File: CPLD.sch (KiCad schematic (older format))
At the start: 35 parts, among them J5 JTAG, SW2 SW_DIP_x06, SW3 User PB, U12 74HCT3G04, U3 EPM7064STC100, X1 CFPS-72 50mhz

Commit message: lots of fixes
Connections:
- net labels added: IEI, IEO
- wire segments 186 -> 187
- no-connect marks 8 -> 6
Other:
- moved on the sheet: C5, D2, J5, R10, R11, R12, R13, R15, R16, R17, R18, RN1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

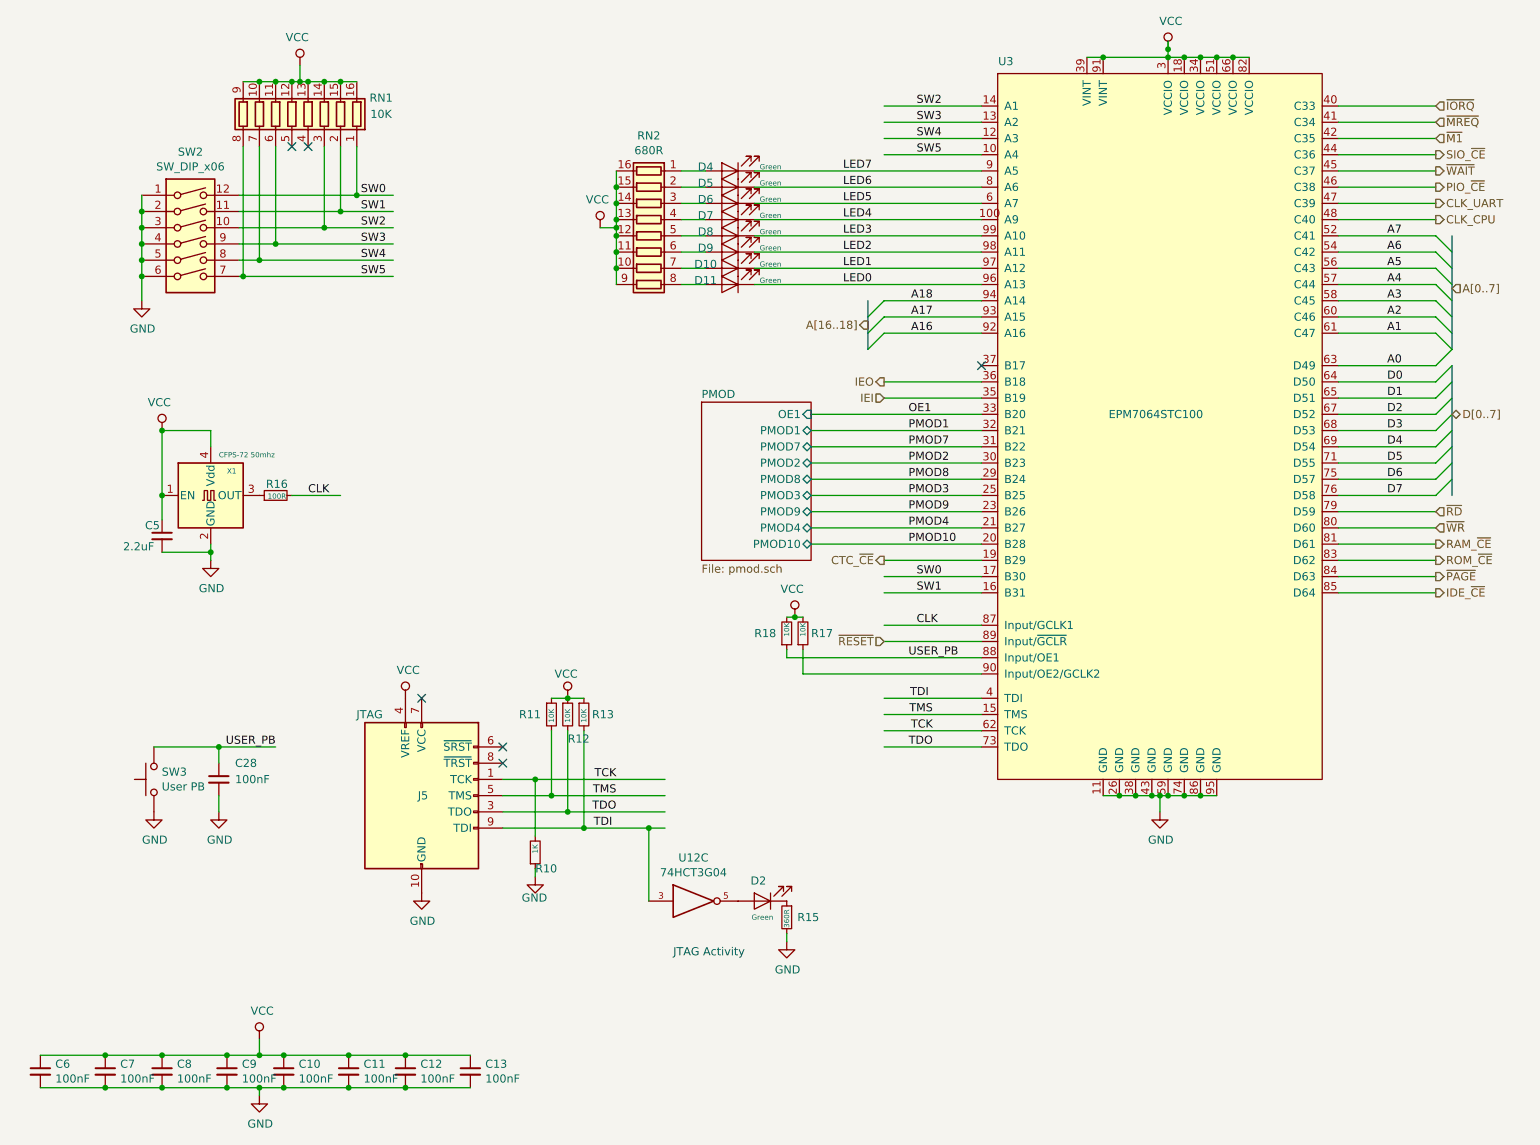
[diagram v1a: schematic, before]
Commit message: fixed led values, added pwr led
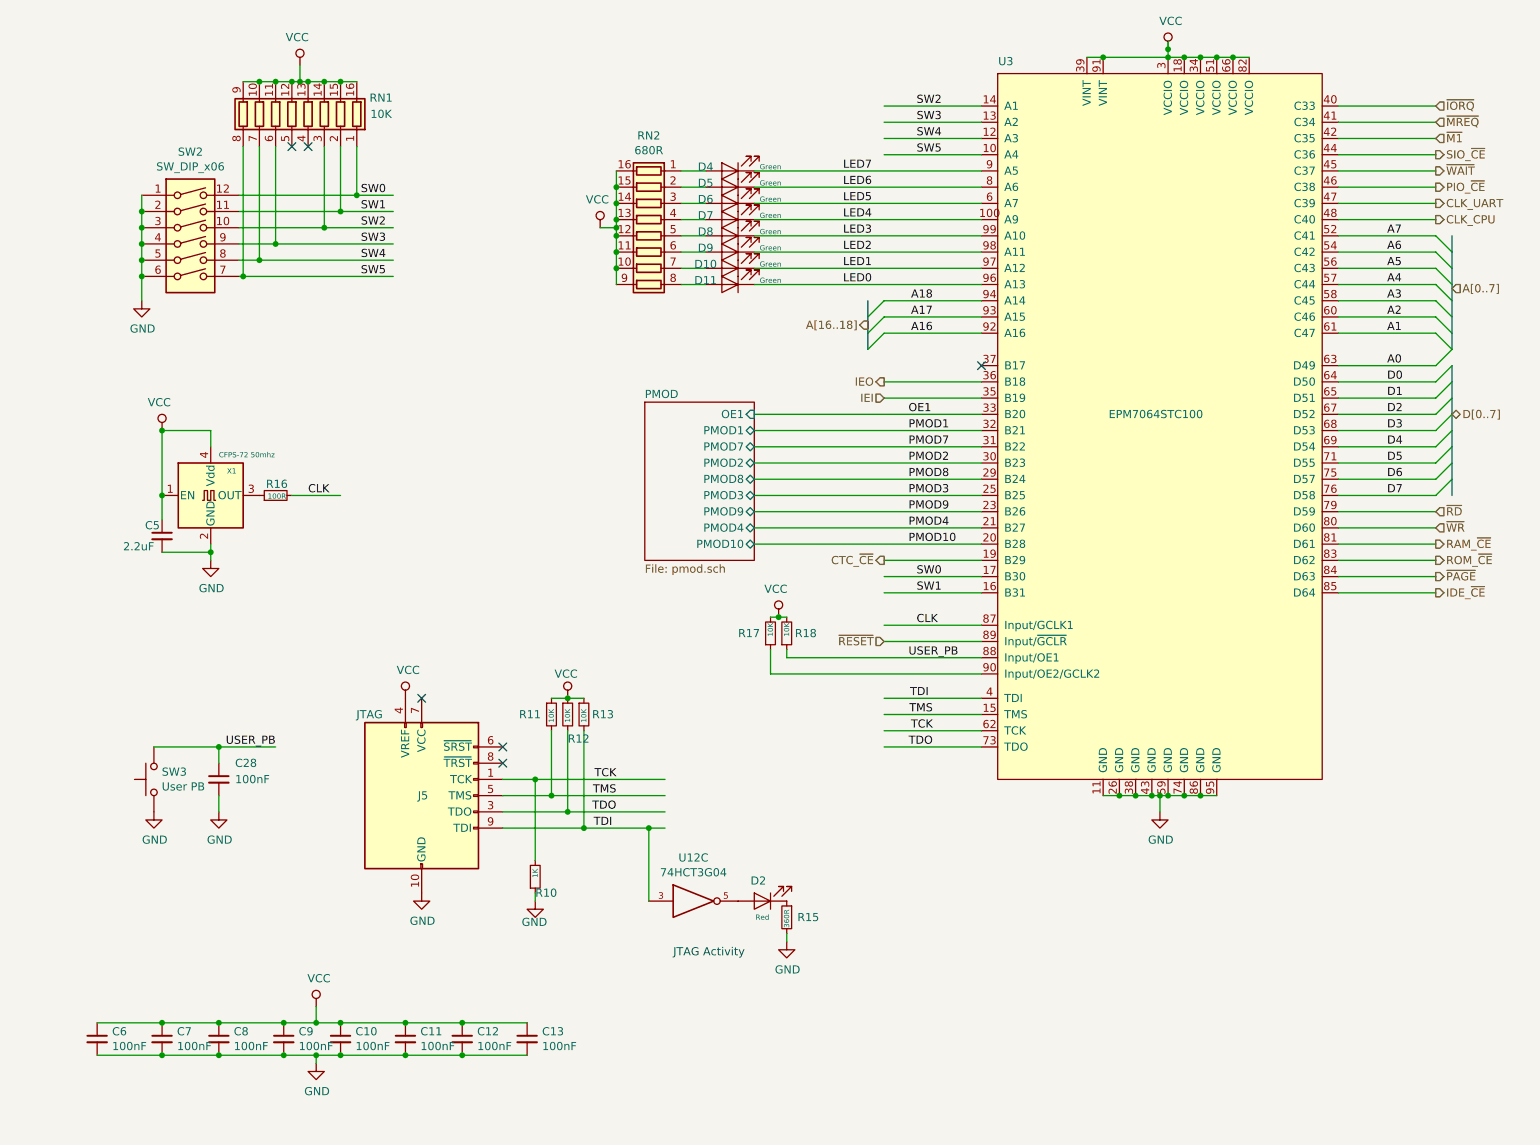
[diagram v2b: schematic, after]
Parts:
- D2: value Green -> Red
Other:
- moved on the sheet: C10, C11, C12, C13, C6, C7, C8, C9, R10, R17

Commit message: lots of fixes
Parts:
- removed R13: 10K, Resistor_SMD:R_0603_1608Metric_Pad1.05x0.95mm_HandSolder, symbol Device:R_Small
- J5: footprint Connector_PinHeader_2.54mm:PinHeader_2x05_P2.54mm_Vertical -> Connector_Multicomp:Multicomp_MC9A12-1034_2x05_P2.54mm_Vertical
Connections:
- wire segments 187 -> 186
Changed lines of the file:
@@
 AR Path="/5DC12F5E" Ref="R?"  Part="1"
 AR Path="/5D70CA34/5DC12F5E" Ref="R10"  Part="1"
-F 0 "R10" H 4000 6100 50  0000 L CNN
+F 0 "R10" H 4050 6000 50  0000 L CNN
 F 1 "1K" V 4000 5950 32  0000 L CNN
 F 2 "Resistor_SMD:R_0603_1608Metric_Pad1.05x0.95mm_HandSolder" H 4000 6000 50  0001 C CNN
@@
 F 0 "J5" H 3340 5500 50  0000 R CNN
 F 1 "JTAG" H 3060 6000 50  0000 R CNN
-F 2 "Connector_PinHeader_2.54mm:PinHeader_2x05_P2.54mm_Vertical" V 3150 5650 50  0001 C CNN
+F 2 "Connector_Multicomp:Multicomp_MC9A12-1034_2x05_P2.54mm_Vertical" V 3150 5650 50  0001 C CNN
 F 3 "~" H 2025 4950 50  0001 C CNN
 	1    3300 5500
@@
 	5450 4600 5450 4750
 $Comp
-L power:VCC #PWR?
-U 1 1 5DC12F7A
-P 4200 4900
-AR Path="/5DC12F7A" Ref="#PWR?"  Part="1"
-AR Path="/5D70CA34/5DC12F7A" Ref="#PWR022"  Part="1"
-F 0 "#PWR022" H 4200 4750 50  0001 C CNN
-F 1 "VCC" H 4190 5050 50  0000 C CNN
-F 2 "" H 4200 4900 50  0001 C CNN
-F 3 "" H 4200 4900 50  0001 C CNN
-	1    4200 4900
-	1    0    0    -1
-$EndComp
-$Comp
-L Device:R_Small R?
-U 1 1 5DC12F74
-P 4300 5000
-AR Path="/5D0F9837/5DC12F74" Ref="R?"  Part="1"
-AR Path="/5CFABACD/5D0BF766/5DC12F74" Ref="R?"  Part="1"
-AR Path="/5D1AF052/5DC12F74" Ref="R?"  Part="1"
-AR Path="/5DC12F74" Ref="R?"  Part="1"
-AR Path="/5D70CA34/5DC12F74" Ref="R13"  Part="1"
-F 0 "R13" H 4350 5000 50  0000 L CNN
-F 1 "10K" V 4300 4950 32  0000 L CNN
-F 2 "Resistor_SMD:R_0603_1608Metric_Pad1.05x0.95mm_HandSolder" H 4300 5000 50  0001 C CNN
-F 3 "~" H 4300 5000 50  0001 C CNN
-	1    4300 5000
-	1    0    0    -1
-$EndComp
-$Comp
 L Device:R_Small R?
 U 1 1 5DC12F6E
@@
 AR Path="/5DC12F6E" Ref="R?"  Part="1"
 AR Path="/5D70CA34/5DC12F6E" Ref="R12"  Part="1"
-F 0 "R12" H 4200 4850 50  0000 L CNN
+F 0 "R12" H 4250 5000 50  0000 L CNN
 F 1 "10K" V 4100 4950 32  0000 L CNN
 F 2 "Resistor_SMD:R_0603_1608Metric_Pad1.05x0.95mm_HandSolder" H 4200 5000 50  0001 C CNN
@@
 $EndComp
 Wire Wire Line
-	3800 5600 4200 5600
-Wire Wire Line
-	3800 5700 4300 5700
-Wire Wire Line
 	3800 5500 4100 5500
 Wire Wire Line
@@
 	4100 5500 4800 5500
 Wire Wire Line
-	4200 5100 4200 5600
-Connection ~ 4200 5600
-Wire Wire Line
-	4200 5600 4800 5600
-Wire Wire Line
-	4300 5100 4300 5700
-Connection ~ 4300 5700
-Wire Wire Line
-	4100 4900 4200 4900
-Connection ~ 4200 4900
-Wire Wire Line
-	4200 4900 4300 4900
-Wire Wire Line
-	4300 5700 4700 5700
+	4100 4900 4150 4900
 Wire Wire Line
 	4700 6150 4700 5700
@@
 Wire Wire Line
 	5450 4750 6750 4750
+Wire Wire Line
+	3800 5700 4200 5700
+$Comp
+L power:VCC #PWR?
+U 1 1 5DA39994
+P 4150 4850
+AR Path="/5DA39994" Ref="#PWR?"  Part="1"
+AR Path="/5D70CA34/5DA39994" Ref="#PWR022"  Part="1"
+F 0 "#PWR022" H 4150 4700 50  0001 C CNN
+F 1 "VCC" H 4167 5023 50  0000 C CNN
+F 2 "" H 4150 4850 50  0001 C CNN
+F 3 "" H 4150 4850 50  0001 C CNN
+	1    4150 4850
+	-1   0    0    -1
+$EndComp
+Wire Wire Line
+	4150 4850 4150 4900
+Connection ~ 4150 4900
+Wire Wire Line
+	4150 4900 4200 4900
+Wire Wire Line
+	3800 5600 4800 5600
+Wire Wire Line
+	4200 5100 4200 5700
+Connection ~ 4200 5700
+Wire Wire Line
+	4200 5700 4700 5700
 Wire Bus Line
 	6050 2450 6050 2750

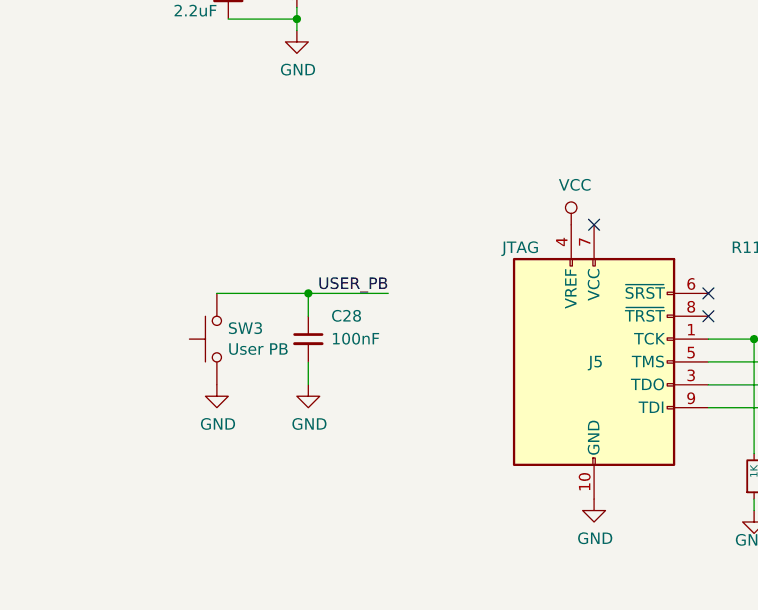
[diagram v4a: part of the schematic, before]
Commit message: added bypass for jtag
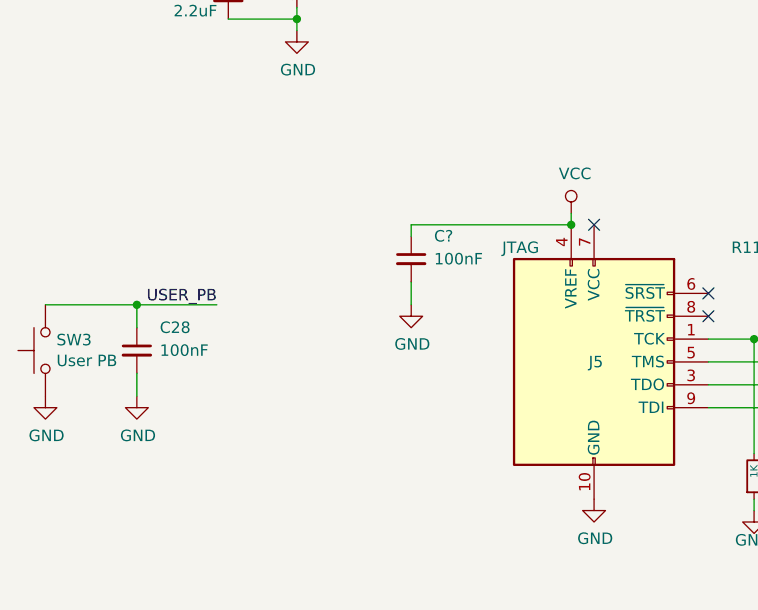
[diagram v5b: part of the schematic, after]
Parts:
- added C?: 100nF, Capacitor_SMD:C_0603_1608Metric_Pad1.05x0.95mm_HandSolder, symbol Device:C_Small
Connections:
- wire segments 186 -> 190
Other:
- moved on the sheet: C28, SW3
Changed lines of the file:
@@
 L power:VCC #PWR?
 U 1 1 5DC12FAB
-P 3200 4900
+P 3200 4850
 AR Path="/5DC12FAB" Ref="#PWR?"  Part="1"
 AR Path="/5D70CA34/5DC12FAB" Ref="#PWR020"  Part="1"
-F 0 "#PWR020" H 3200 4750 50  0001 C CNN
-F 1 "VCC" H 3217 5073 50  0000 C CNN
-F 2 "" H 3200 4900 50  0001 C CNN
-F 3 "" H 3200 4900 50  0001 C CNN
-	1    3200 4900
+F 0 "#PWR020" H 3200 4700 50  0001 C CNN
+F 1 "VCC" H 3217 5023 50  0000 C CNN
+F 2 "" H 3200 4850 50  0001 C CNN
+F 3 "" H 3200 4850 50  0001 C CNN
+	1    3200 4850
 	1    0    0    -1
 $EndComp
@@
 L Switch:SW_Push SW3
 U 1 1 5D8710D3
-P 1650 5400
-F 0 "SW3" V 1696 5352 50  0000 R CNN
-F 1 "User PB" V 1605 5352 50  0000 R CNN
-F 2 "Button_Switch_SMD:SW_SPST_FSMSM" H 1650 5600 50  0001 C CNN
-F 3 "~" H 1650 5600 50  0001 C CNN
-	1    1650 5400
+P 900 5450
+F 0 "SW3" V 946 5402 50  0000 R CNN
+F 1 "User PB" V 855 5402 50  0000 R CNN
+F 2 "Button_Switch_SMD:SW_SPST_FSMSM" H 900 5650 50  0001 C CNN
+F 3 "~" H 900 5650 50  0001 C CNN
+	1    900  5450
 	0    -1   -1   0
 $EndComp
@@
 L power:GND #PWR082
 U 1 1 5D8738FA
-P 1650 5600
-F 0 "#PWR082" H 1650 5350 50  0001 C CNN
-F 1 "GND" H 1655 5427 50  0000 C CNN
-F 2 "" H 1650 5600 50  0001 C CNN
-F 3 "" H 1650 5600 50  0001 C CNN
-	1    1650 5600
-	1    0    0    -1
-$EndComp
-Wire Wire Line
-	1650 5200 2050 5200
+P 900 5650
+F 0 "#PWR082" H 900 5400 50  0001 C CNN
+F 1 "GND" H 905 5477 50  0000 C CNN
+F 2 "" H 900 5650 50  0001 C CNN
+F 3 "" H 900 5650 50  0001 C CNN
+	1    900  5650
+	1    0    0    -1
+$EndComp
+Wire Wire Line
+	900  5250 1300 5250
 $Comp
 L Device:C_Small C?
 U 1 1 5D88E389
-P 2050 5400
+P 1300 5450
 AR Path="/5D65A6A0/5D88E389" Ref="C?"  Part="1"
 AR Path="/5D88E389" Ref="C?"  Part="1"
 AR Path="/5D70CA34/5D88E389" Ref="C28"  Part="1"
-F 0 "C28" H 2150 5500 50  0000 L CNN
-F 1 "100nF" H 2150 5400 50  0000 L CNN
-F 2 "Capacitor_SMD:C_0603_1608Metric_Pad1.05x0.95mm_HandSolder" H 2050 5400 50  0001 C CNN
-F 3 "https://www.mouser.com/datasheet/2/396/mlcc02_e-1307760.pdf" H 2050 5400 50  0001 C CNN
-F 4 "Multilayer Ceramic Capacitors MLCC - SMD/SMT 0603 10V 10nF 5% X7R" H 2142 5546 50  0001 C CNN "Description"
-F 5 "Taiyo Yuden" H 2050 5400 50  0001 C CNN "MFR"
-F 6 "JMK107B7474KA-T" H 2050 5400 50  0001 C CNN "MPN"
-F 7 "963-JMK107B7474KA-T" H 2142 5546 50  0001 C CNN "SPN"
-F 8 "Mouser" H 2050 5400 50  0001 C CNN "SPR"
-F 9 "https://www.mouser.com/ProductDetail/963-JMK107B7474KA-T" H 2142 5546 50  0001 C CNN "SPURL"
-	1    2050 5400
-	1    0    0    -1
-$EndComp
-Wire Wire Line
-	2050 5300 2050 5200
+F 0 "C28" H 1400 5550 50  0000 L CNN
+F 1 "100nF" H 1400 5450 50  0000 L CNN
+F 2 "Capacitor_SMD:C_0603_1608Metric_Pad1.05x0.95mm_HandSolder" H 1300 5450 50  0001 C CNN
+F 3 "https://www.mouser.com/datasheet/2/396/mlcc02_e-1307760.pdf" H 1300 5450 50  0001 C CNN
+F 4 "Multilayer Ceramic Capacitors MLCC - SMD/SMT 0603 10V 10nF 5% X7R" H 1392 5596 50  0001 C CNN "Description"
+F 5 "Taiyo Yuden" H 1300 5450 50  0001 C CNN "MFR"
+F 6 "JMK107B7474KA-T" H 1300 5450 50  0001 C CNN "MPN"
+F 7 "963-JMK107B7474KA-T" H 1392 5596 50  0001 C CNN "SPN"
+F 8 "Mouser" H 1300 5450 50  0001 C CNN "SPR"
+F 9 "https://www.mouser.com/ProductDetail/963-JMK107B7474KA-T" H 1392 5596 50  0001 C CNN "SPURL"
+	1    1300 5450
+	1    0    0    -1
+$EndComp
+Wire Wire Line
+	1300 5350 1300 5250
 $Comp
 L power:GND #PWR083
 U 1 1 5D8C3559
-P 2050 5600
-F 0 "#PWR083" H 2050 5350 50  0001 C CNN
-F 1 "GND" H 2055 5427 50  0000 C CNN
-F 2 "" H 2050 5600 50  0001 C CNN
-F 3 "" H 2050 5600 50  0001 C CNN
-	1    2050 5600
-	1    0    0    -1
-$EndComp
-Wire Wire Line
-	2050 5500 2050 5600
-Text Label 2400 5200 2    50   ~ 0
+P 1300 5650
+F 0 "#PWR083" H 1300 5400 50  0001 C CNN
+F 1 "GND" H 1305 5477 50  0000 C CNN
+F 2 "" H 1300 5650 50  0001 C CNN
+F 3 "" H 1300 5650 50  0001 C CNN
+	1    1300 5650
+	1    0    0    -1
+$EndComp
+Wire Wire Line
+	1300 5550 1300 5650
+Text Label 1650 5250 2    50   ~ 0
 USER_PB
-Connection ~ 2050 5200
-Wire Wire Line
-	2050 5200 2400 5200
+Connection ~ 1300 5250
+Wire Wire Line
+	1300 5250 1650 5250
 $Sheet
 S 4675 3075 675  975
@@
 Wire Wire Line
 	4200 5700 4700 5700
+$Comp
+L Device:C_Small C?
+U 1 1 5D8DCE07
+P 2500 5050
+AR Path="/5D65A6A0/5D8DCE07" Ref="C?"  Part="1"
+AR Path="/5D8DCE07" Ref="C?"  Part="1"
+AR Path="/5D70CA34/5D8DCE07" Ref="C?"  Part="1"
+F 0 "C?" H 2600 5150 50  0000 L CNN
+F 1 "100nF" H 2600 5050 50  0000 L CNN
+F 2 "Capacitor_SMD:C_0603_1608Metric_Pad1.05x0.95mm_HandSolder" H 2500 5050 50  0001 C CNN
+F 3 "https://www.mouser.com/datasheet/2/396/mlcc02_e-1307760.pdf" H 2500 5050 50  0001 C CNN
+F 4 "Multilayer Ceramic Capacitors MLCC - SMD/SMT 0603 10V 10nF 5% X7R" H 2592 5196 50  0001 C CNN "Description"
+F 5 "Taiyo Yuden" H 2500 5050 50  0001 C CNN "MFR"
+F 6 "JMK107B7474KA-T" H 2500 5050 50  0001 C CNN "MPN"
+F 7 "963-JMK107B7474KA-T" H 2592 5196 50  0001 C CNN "SPN"
+F 8 "Mouser" H 2500 5050 50  0001 C CNN "SPR"
+F 9 "https://www.mouser.com/ProductDetail/963-JMK107B7474KA-T" H 2592 5196 50  0001 C CNN "SPURL"
+	1    2500 5050
+	1    0    0    -1
+$EndComp
+$Comp
+L power:GND #PWR?
+U 1 1 5D8DCE0D
+P 2500 5250
+F 0 "#PWR?" H 2500 5000 50  0001 C CNN
+F 1 "GND" H 2505 5077 50  0000 C CNN
+F 2 "" H 2500 5250 50  0001 C CNN
+F 3 "" H 2500 5250 50  0001 C CNN
+	1    2500 5250
+	1    0    0    -1
+$EndComp
+Wire Wire Line
+	2500 5150 2500 5250
+Wire Wire Line
+	3200 4900 3200 4850
+Wire Wire Line
+	2500 4950 2500 4900
+Wire Wire Line
+	2500 4900 3200 4900
 Wire Bus Line
 	6050 2450 6050 2750
@@
 Wire Bus Line
 	9650 2850 9650 3650
+Connection ~ 3200 4900
 $EndSCHEMATC

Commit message: rerouting
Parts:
- gave numbers to parts that had none: 1
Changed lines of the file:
@@
 AR Path="/5D65A6A0/5D8DCE07" Ref="C?"  Part="1"
 AR Path="/5D8DCE07" Ref="C?"  Part="1"
-AR Path="/5D70CA34/5D8DCE07" Ref="C?"  Part="1"
-F 0 "C?" H 2600 5150 50  0000 L CNN
+AR Path="/5D70CA34/5D8DCE07" Ref="C30"  Part="1"
+F 0 "C30" H 2600 5150 50  0000 L CNN
 F 1 "100nF" H 2600 5050 50  0000 L CNN
 F 2 "Capacitor_SMD:C_0603_1608Metric_Pad1.05x0.95mm_HandSolder" H 2500 5050 50  0001 C CNN
@@
 $EndComp
 $Comp
-L power:GND #PWR?
+L power:GND #PWR0106
 U 1 1 5D8DCE0D
 P 2500 5250
-F 0 "#PWR?" H 2500 5000 50  0001 C CNN
+F 0 "#PWR0106" H 2500 5000 50  0001 C CNN
 F 1 "GND" H 2505 5077 50  0000 C CNN
 F 2 "" H 2500 5250 50  0001 C CNN
@@
 Wire Wire Line
 	2500 4900 3200 4900
+Connection ~ 3200 4900
 Wire Bus Line
 	6050 2450 6050 2750
@@
 Wire Bus Line
 	9650 2850 9650 3650
-Connection ~ 3200 4900
 $EndSCHEMATC
